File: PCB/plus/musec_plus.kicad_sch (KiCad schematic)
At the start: 63 parts, among them J1 Pedal, J2 PJ313, J3 PJ313, SW1 SW_DIP_x01, SW2 SW_DIP_x01, SW3 SW_DIP_x01, SW4 SW_DIP_x01, SW5 SW_DIP_x01, SW6 SW_DIP_x01, SW7 SW_DIP_x01, U1 PiPico, U3 TMAG5273, U4 TMAG5273, U5 TMAG5273, U6 TMAG5273, U7 TMAG5273

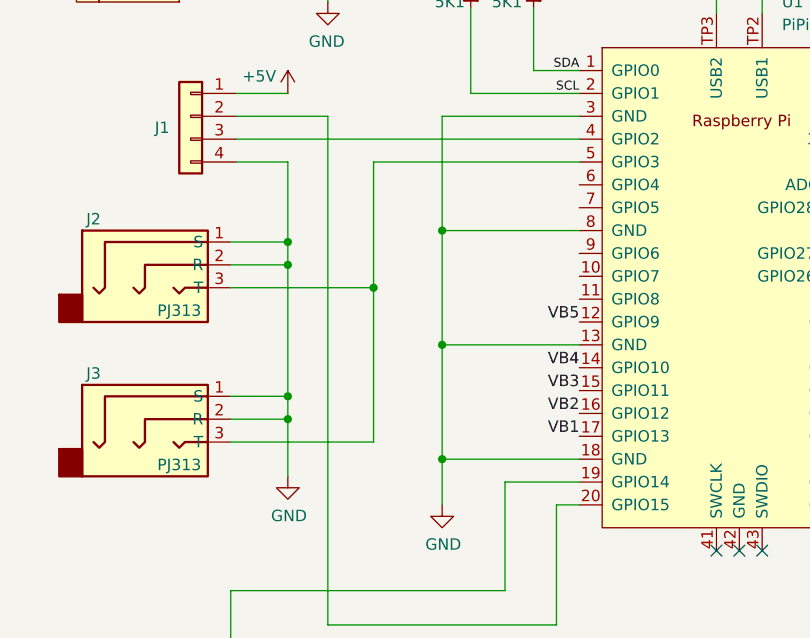
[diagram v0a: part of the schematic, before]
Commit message: PCB V1.2, add pedal TRS ring option
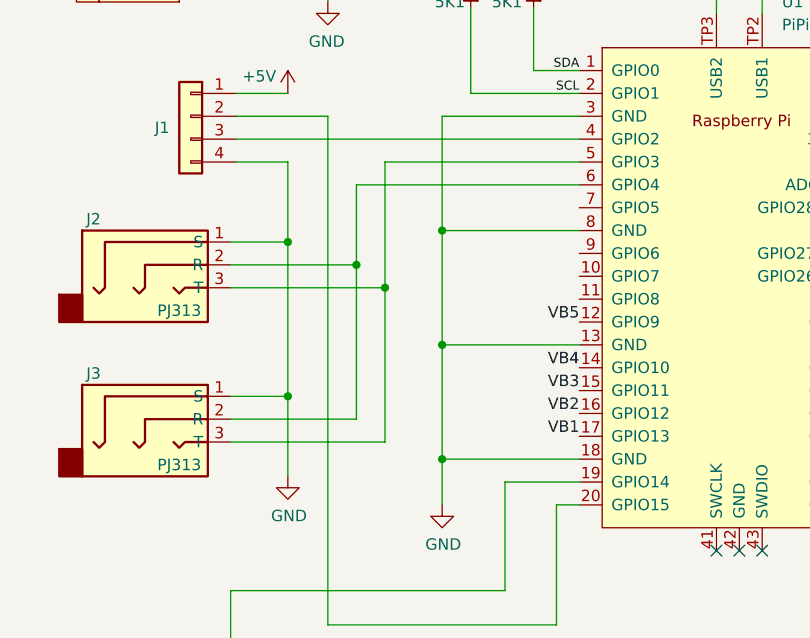
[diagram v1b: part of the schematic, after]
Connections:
- net GND: no longer J2.2 (R), J3.2 (R)
- net at U1.6 (GPIO4): now also J2.2 (R), J3.2 (R)
